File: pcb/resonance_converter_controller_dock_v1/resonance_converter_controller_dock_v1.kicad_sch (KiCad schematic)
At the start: 157 parts, among them J1 FX18-120S-0.8SV15, J10 Conn_Coaxial, J11 Conn_01x02, J12 Conn_01x02, J13 Conn_Coaxial, J14 Conn_Coaxial, J15 Conn_01x02, J16 Conn_01x02, J17 Conn_Coaxial, J18 Conn_01x02, J19 Conn_01x04, J2 Conn_01x52_MountingPin, J20 Conn_01x04, J21 Conn_01x04, J22 Conn_01x06, J23 Conn_Coaxial, J24 Conn_01x02, J25 Conn_01x02, J26 Conn_Coaxial, J27 Conn_01x04, J28 Conn_01x02, J29 USB_C_Receptacle_USB2.0_14P, J3 Conn_Coaxial, J30 Conn_01x09, J31 Conn_01x04_MountingPin, J32 Conn_01x04_MountingPin, J33 Conn_01x04_MountingPin, J34 Conn_02x05_Odd_Even, J4 Conn_01x02, J5 Conn_Coaxial, J6 Conn_01x02, J7 Conn_Coaxial, J8 Conn_01x02, J9 Conn_Coaxial, M1 Fan_4pin, SW1 RotaryEncoder_Switch_MP, SW2 SW_SPST, SW3 SW_SPST, SW4 SW_SPST, SW5 SW_SPST, SW6 SW_SPST, U1 STM32F105R8Tx, U10 TMUX131RMG, U11 TMUX131RMG, U12 TMUX131RMG, U13 TMUX131RMG, U14 TMUX131RMG, U15 TMUX154ERSW, U16 AT24CS32-XHM, U17 TMUX1574RSV, U18 TMUX1574RSV, U19 TMUX131RMG, U2 FUSB302B01MPX, U20 TMUX1574RSV, U21 TMUX154ERSW, U22 TMUX154ERSW, U23 TMUX154ERSW, U24 BTS5012SDA, U25 BTS5012SDA, U26 BTS5012SDA, U27 74LVC1G04, U3 LM2576HVS-ADJ, U4 TMUX131RMG, U5 LM7812_TO220, U6 TPS2116DRL, U7 AZ1117-3.3, U8 AP2171W, U9 TMUX131RMG, Y1 16Mhz

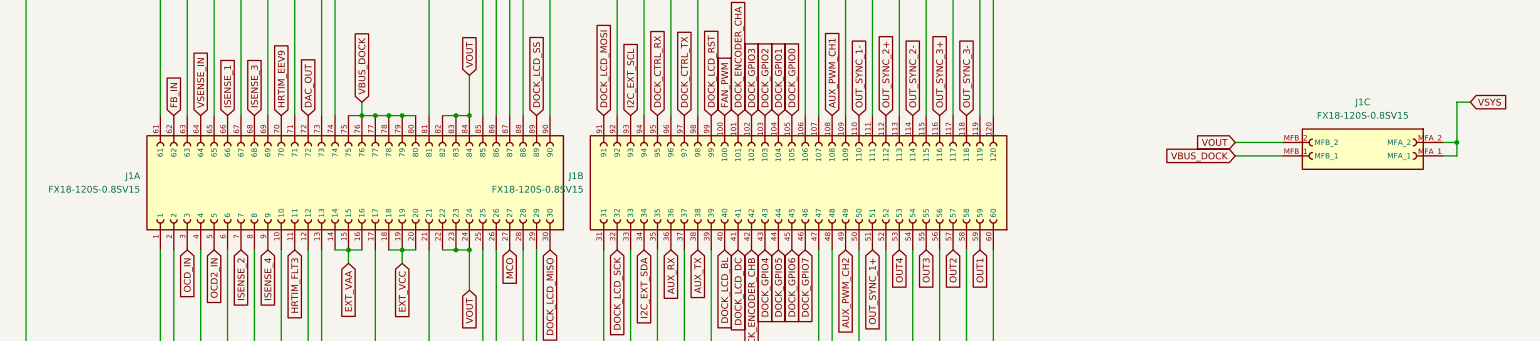
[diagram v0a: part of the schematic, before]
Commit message: Update conector in dock
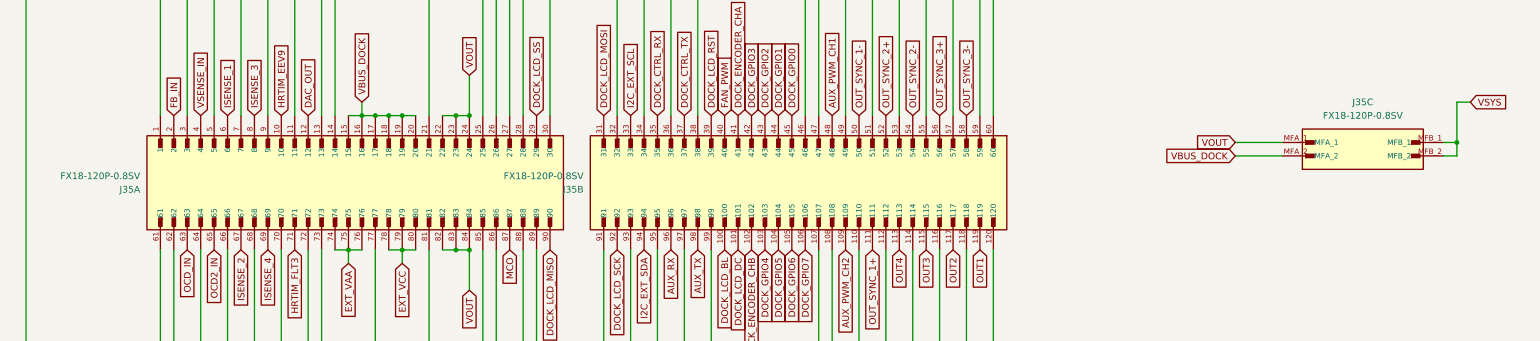
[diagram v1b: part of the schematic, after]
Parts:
- removed J1: FX18-120S-0.8SV15, FX18-120S-0.8SV15:HIROSE_FX18-120S-0.8SV15, symbol FX18-120S-0.8SV15:FX18-120S-0.8SV15
- added J35: FX18-120P-0.8SV, FX18-120P-0.8SV:HIROSE_FX18-120P-0.8SV, symbol FX18-120P-0.8SV:FX18-120P-0.8SV
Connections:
- net AUX_PWM_CH1: now also J35.48
- net AUX_PWM_CH2: now also J35.109
- net AUX_RX: now also J35.96
- net AUX_TX: now also J35.98
- net DAC_OUT: now also J35.12
- net DOCK_CTRL_RX: now also J35.35
- net DOCK_CTRL_TX: now also J35.37
- net DOCK_ENCODER_CHA: now also J35.41
- net DOCK_ENCODER_CHB: now also J35.102
- net DOCK_GPIO0: now also J35.45
- net DOCK_GPIO1: now also J35.44
- net DOCK_GPIO2: now also J35.43
- net DOCK_GPIO3: now also J35.42
- net DOCK_GPIO4: now also J35.103
- net DOCK_GPIO5: now also J35.104
- net DOCK_GPIO6: now also J35.105
- net DOCK_GPIO7: now also J35.106
- net DOCK_LCD_BL: now also J35.100
- net DOCK_LCD_DC: now also J35.101
- net DOCK_LCD_MISO: now also J35.90
- net DOCK_LCD_MOSI: now also J35.31
- net DOCK_LCD_RST: now also J35.39
- net DOCK_LCD_SCK: now also J35.92
- net DOCK_LCD_SS: now also J35.29
- net EXT_VAA: now also J35.74, J35.75, J35.76
- net EXT_VCC: now also J35.78, J35.79, J35.80
- net FAN_PWM: now also J35.40
- net FB_IN: now also J35.2
- net GND: now also J35.1, J35.107, J35.108, J35.11, J35.110, J35.112, J35.114, J35.116, J35.118, J35.120, J35.13, J35.14, J35.21, J35.25, J35.26, J35.27, J35.28, J35.3, J35.30, J35.32, J35.34, J35.36, J35.38, J35.46, J35.47, J35.49, J35.5, J35.51, J35.53, J35.55, J35.57, J35.59, J35.60, J35.61, J35.62, J35.64, J35.66, J35.68, J35.7, J35.70, J35.72, J35.73, J35.77, J35.81, J35.85, J35.86, J35.88, J35.89, J35.9, J35.91, J35.93, J35.95, J35.97, J35.99
- net HRTIM_EEV9: now also J35.10
- net HRTIM_FLT3: now also J35.71
- net I2C_EXT_SCL: now also J35.33
- net I2C_EXT_SDA: now also J35.94
- net ISENSE_1: now also J35.6
- net ISENSE_2: now also J35.67
- net ISENSE_3: now also J35.8
- net ISENSE_4: now also J35.69
- net MCO: now also J35.87
- net OCD2_IN: now also J35.65
- net OCD_IN: now also J35.63
- net OUT1: now also J35.119
- net OUT2: now also J35.117
- net OUT3: now also J35.115
- net OUT4: now also J35.113
- net OUT_SYNC_1+: now also J35.111
- net OUT_SYNC_1-: now also J35.50
- net OUT_SYNC_2+: now also J35.52
- net OUT_SYNC_2-: now also J35.54
- net OUT_SYNC_3+: now also J35.56
- net OUT_SYNC_3-: now also J35.58
- net VBUS: now also J35.15, J35.16, J35.17, J35.18, J35.19, J35.20, J35.MFA_2
- net VOUT: now also J35.22, J35.23, J35.24, J35.82, J35.83, J35.84, J35.MFA_1
- net VSENSE_IN: now also J35.4
- net VSYS: now also J35.MFB_1, J35.MFB_2

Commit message: Fix errors and make initial component placement in dock
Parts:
- removed C21: C_Polarized, Capacitor_SMD:CP_Elec_5x4.5, symbol Device:C_Polarized
- removed J31, J32, J33: Conn_01x04_MountingPin, Connector_JST:JST_PH_S4B-PH-SM4-TB_1x04-1MP_P2.00mm_Horizontal, symbol Connector_Generic_MountingPin:Conn_01x04_MountingPin
- added C21: C, Capacitor_SMD:C_0402_1005Metric, symbol Device:C
- added C48: 100nF, Capacitor_SMD:C_0402_1005Metric, symbol Device:C
- added J1, J31, J32: Conn_01x04, Connector_JST:JST_PH_S4B-PH-K_1x04_P2.00mm_Horizontal, symbol Connector_Generic:Conn_01x04
- C10, C14, C20, C31, C32, C36, C43, C44, C45, C79, C80: footprint Capacitor_SMD:C_0805_2012Metric -> Capacitor_SMD:C_0402_1005Metric
- C8: value 100nF -> C
- R10, R16, R17, R22, R25, R26, R27, R45, R46, R47, R48, R49, R9: footprint Resistor_SMD:R_0805_2012Metric -> Resistor_SMD:R_0402_1005Metric
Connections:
- net SOMLCD_SCK is gone; now on net SOM_LCD_SCK: U10.7 (S1A)
- net +12V: now also C8.1, J1.3 (Pin_3), J31.3 (Pin_3), J32.3 (Pin_3)
- net +3.3V: now also C12.1, C13.1, C17.1, C18.1, C19.1, J1.2 (Pin_2), J31.2 (Pin_2), J32.2 (Pin_2)
- net DEV_PAD_CENTER: now also C48.1
- net GND: now also C21.2, C48.2, J1.4 (Pin_4), J31.4 (Pin_4), J32.4 (Pin_4)
- net VBUS: now also C21.1
- net at R46.2, U24.1 (OUT), U24.5 (OUT): now also J1.1 (Pin_1)
- net at R48.2, U26.1 (OUT), U26.5 (OUT): now also J32.1 (Pin_1)
- net at C20.1, C9.1, D1.1 (+)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: no longer C8.1
- net at R45.2, U25.1 (OUT), U25.5 (OUT): now also J31.1 (Pin_1)

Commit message: Add mounting holes and some rework
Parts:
- added C49, C51: C, Capacitor_SMD:C_2220_5750Metric, symbol Device:C
- added C50: C_Polarized, Capacitor_THT:CP_Radial_D10.0mm_P5.00mm_P7.50mm, symbol Device:C_Polarized
- added H1, H2, H3, H4: MountingHole_Pad, MountingHole:MountingHole_3.2mm_M3_Pad_Via, symbol Mechanical:MountingHole_Pad
- added R20, R21: R, Resistor_THT:R_Axial_Power_L20.0mm_W6.4mm_P22.40mm, symbol Device:R
- U5, U7: footprint Package_TO_SOT_THT:TO-220-3_Vertical -> Package_TO_SOT_SMD:TO-263-2
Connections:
- net VCC is gone; now on net +3.3V: J27.1 (Pin_1), R2.1, R3.1, R4.1, R5.1, R6.1, R7.1, R8.1
- net +12V: no longer C8.1, U7.3 (VI)
- net +3.3V: now also U20.14 (VDD), C50.1, C51.1
- net CTRL_RXTX_FWD_REMOTE: now also U1.10 (PC2); no longer U1.9 (PC1)
- net DEV_CTRL_RX: now also U15.3 (A); no longer U15.5 (B)
- net DEV_CTRL_TX: now also U15.5 (B); no longer U15.3 (A)
- net DEV_ENCODER_A: now also C7.1, R8.2, SW1.A
- net DEV_ENCODER_B: now also C6.1, R7.2, SW1.B
- net DOCK_CTRL_RX: now also U22.3 (A); no longer U22.5 (B)
- net DOCK_CTRL_TX: now also U22.5 (B); no longer U22.3 (A)
- net DOCK_ENCODER_CHA: no longer C7.1, R8.2, SW1.A
- net DOCK_ENCODER_CHB: no longer C6.1, R7.2, SW1.B
- net DOCK_GPIO0: now also U20.10 (D4); no longer U20.2 (D1)
- net DOCK_GPIO1: now also U20.7 (D3); no longer U20.5 (D2)
- net DOCK_GPIO2: now also U20.5 (D2); no longer U20.7 (D3)
- net DOCK_GPIO3: now also U20.2 (D1); no longer U20.10 (D4)
- net DOCK_LCD_BL: now also U18.5 (D2); no longer U18.7 (D3)
- net DOCK_LCD_DC: now also U18.7 (D3); no longer U18.5 (D2)
- net DOCK_LCD_MOSI: now also U17.10 (D4); no longer U17.2 (D1)
- net DOCK_LCD_SS: now also U17.2 (D1); no longer U17.10 (D4)
- net ENCODER_BUS_SELECT_0: now also U1.38 (PC7); no longer U1.37 (PC6)
- net ENCODER_BUS_SELECT_1: now also U1.37 (PC6); no longer U1.38 (PC7)
- net FROM_REMOTE_CTRL_RX: now also U15.2 (A1); no longer U15.6 (B1)
- net FROM_REMOTE_CTRL_TX: now also U15.6 (B1); no longer U15.2 (A1)
- net GND: now also C49.2, C50.2, C51.2, H1.1, H2.1, H3.1, H4.1, R20.2, R21.2
- net LCD_BUS_SELECT_0: now also U1.40 (PC9); no longer U1.39 (PC8)
- net LCD_BUS_SELECT_1: now also U1.39 (PC8); no longer U1.40 (PC9)
- net OCD2_IN: now also R21.1
- net OCD_IN: now also R20.1
- net PAD_BUS_SELECT_0: now also U1.36 (PB15); no longer U1.35 (PB14)
- net PAD_BUS_SELECT_1: now also U1.35 (PB14); no longer U1.36 (PB15)
- net PAD_FWD_REMOTE: now also U1.9 (PC1); no longer U1.10 (PC2)
- net SOM_CTRL_RX: now also U15.1 (A0), U22.1 (A0); no longer U15.7 (B0), U22.7 (B0)
- net SOM_CTRL_TX: now also U15.7 (B0), U22.7 (B0); no longer U15.1 (A0), U22.1 (A0)
- net SOM_LCD_BL: now also U18.3 (S2A); no longer U18.9 (S3A)
- net SOM_LCD_DC: now also U18.9 (S3A); no longer U18.3 (S2A)
- net SOM_LCD_MOSI: now also U17.12 (S4A); no longer U17.16 (S1A)
- net SOM_LCD_SS: now also U17.16 (S1A); no longer U17.12 (S4A)
- net SOM_PAD_DOWN: now also U20.9 (S3A); no longer U20.3 (S2A)
- net SOM_PAD_LEFT: now also U20.3 (S2A); no longer U20.9 (S3A)
- net SOM_PAD_RIGHT: now also U20.16 (S1A); no longer U20.12 (S4A)
- net SOM_PAD_UP: now also U20.12 (S4A); no longer U20.16 (S1A)
- net TO_REMOTE_CTRL_RX: now also U22.2 (A1); no longer U22.6 (B1)
- net TO_REMOTE_CTRL_TX: now also U22.6 (B1); no longer U22.2 (A1)
- net TO_REMOTE_LCD_BL: now also U18.4 (S2B); no longer U18.8 (S3B)
- net TO_REMOTE_LCD_DC: now also U18.8 (S3B); no longer U18.4 (S2B)
- net TO_REMOTE_LCD_MOSI: now also U17.11 (S4B); no longer U17.1 (S1B)
- net TO_REMOTE_LCD_SS: now also U17.1 (S1B); no longer U17.11 (S4B)
- net TO_REMOTE_PAD_DOWN: now also U20.8 (S3B); no longer U20.4 (S2B)
- net TO_REMOTE_PAD_LEFT: now also U20.4 (S2B); no longer U20.8 (S3B)
- net TO_REMOTE_PAD_RIGHT: now also U20.1 (S1B); no longer U20.11 (S4B)
- net TO_REMOTE_PAD_UP: now also U20.11 (S4B); no longer U20.1 (S1B)
- net VBUS: now also C8.1, U7.3 (VI), C49.1
- net PUSB+: now reaches R12.1, U1.45 (PA12)
- net PUSB-: now reaches R11.1, U1.44 (PA11)
